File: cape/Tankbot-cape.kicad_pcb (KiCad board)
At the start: 2 copper layers, 54.6 x 86.4 mm, 17 parts, among them J1 MOTOR_RIBBON, J2 Battery, J3 Regulator connector, J4 JUMP TO DISABLE REGULATOR, J5 Qwiic Connector, P8 BeagleBone_Black_Header, P9 BeagleBone_Black_Header

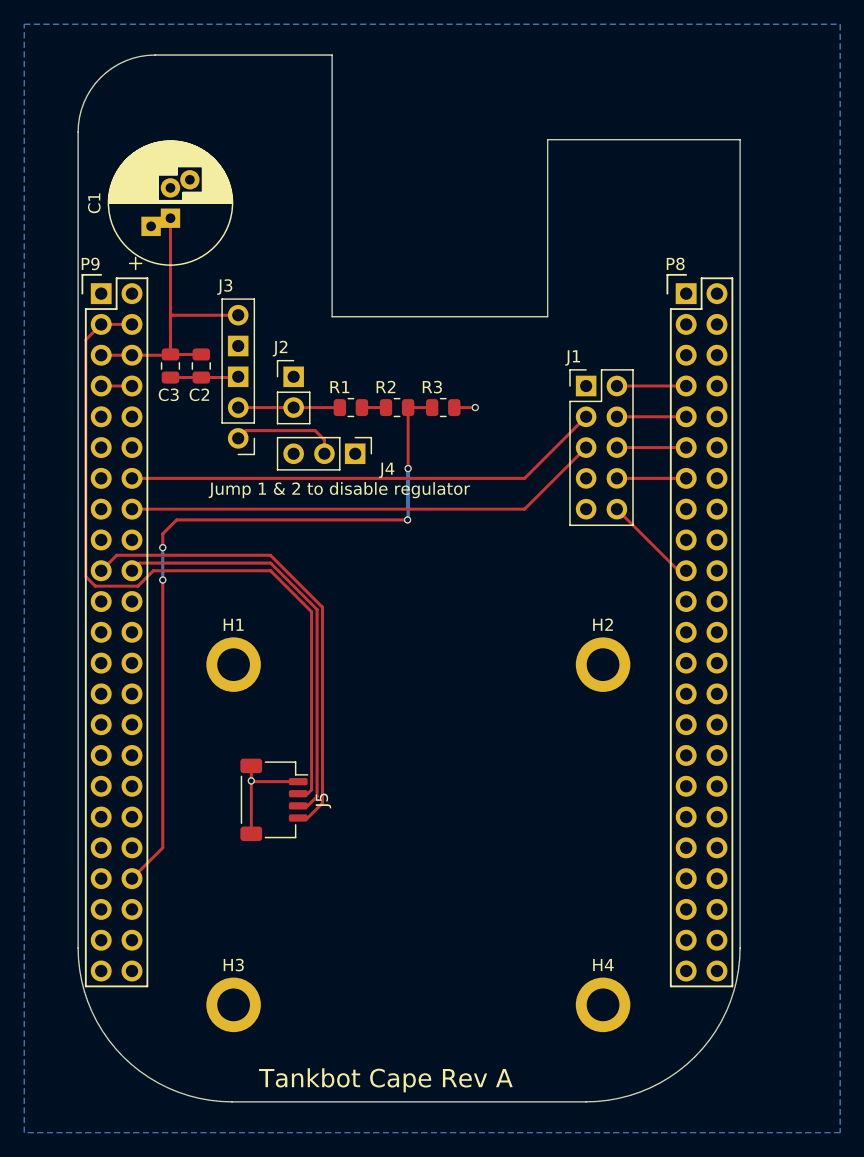
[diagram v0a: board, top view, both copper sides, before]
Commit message: Dropped regulator disable, fixed battery footprint, etc
1. I removed the regulator disable header as I don't think it's necessary.
1. I fixed the battery footprint to be an XT30 connector.
1. I gave the motor ribbon connector a little more clearance to P8.
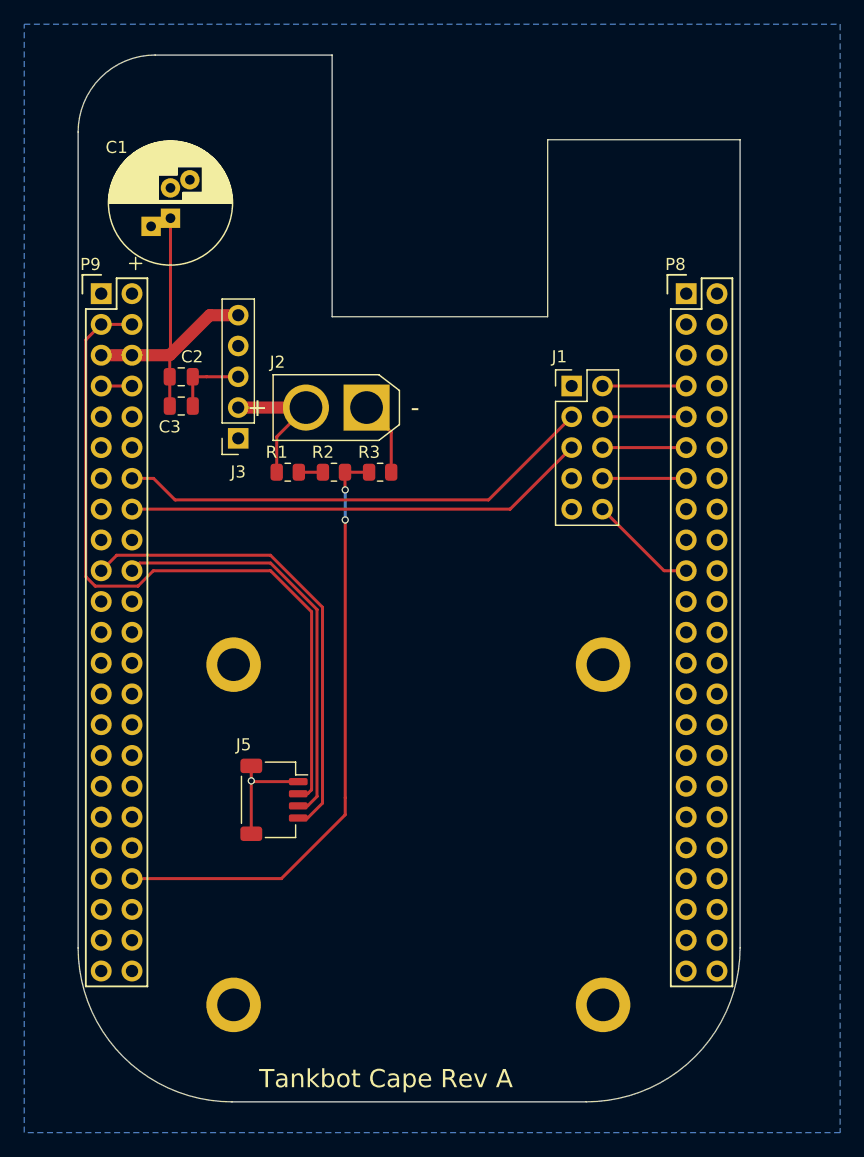
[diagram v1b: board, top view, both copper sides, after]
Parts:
- removed J4: JUMP TO DISABLE REGULATOR, Connector_PinHeader_2.54mm:PinHeader_1x03_P2.54mm_Vertical
- J2: footprint Connector_PinHeader_2.54mm:PinHeader_1x02_P2.54mm_Vertical -> Connector_AMASS:AMASS_XT30U-M_1x02_P5.0mm_Vertical
- J3: footprint Connector_PinHeader_2.54mm:PinHeader_1x05_P2.54mm_Vertical -> Connector_PinSocket_2.54mm:PinSocket_1x05_P2.54mm_Vertical
- moved R3 7.45 mm to (139.4, 77.1)
- moved R1 7.45 mm to (131.8, 77.1)
- moved R2 7.45 mm to (135.6, 77.1)
- moved J2 6.53 mm to (138.3, 71.8), turned to 180 degrees
- moved C3 3.42 mm to (123.0, 71.7), turned to 0 degrees
- moved C2 1.88 mm to (123.0, 69.2), turned to 0 degrees
- moved J1 1.19 mm to (155.2, 70.0)
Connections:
- J3 pad 1: REGULATOR_ENABLE -> Net-(J3-Pad1)
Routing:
- net VBAT_MEASURE: track 64.9 -> 50.0 mm, vias 4 -> 2
- net REGULATOR_ENABLE: track 8.83 -> 0.00 mm
- net GNDD: track 17.0 -> 22.2 mm, vias 2 -> 1
- net +BATT: track 8.38 -> 11.9 mm
- net MOTOR_RIGHT_B: track 7.82 -> 9.65 mm
- net +5V: track 29.6 -> 31.2 mm
- net MOTOR_LEFT_B: track 39.6 -> 38.4 mm
- net MOTOR_nSLEEP: track 5.72 -> 6.91 mm
- net MOTOR_nFAULT: track 5.72 -> 6.91 mm
- net MOTOR_RIGHT_A: track 5.72 -> 6.91 mm
- net MOTOR_PWR_EN: track 5.72 -> 6.91 mm
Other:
- board text removed: "Jump 1 & 2 to disable regulator"

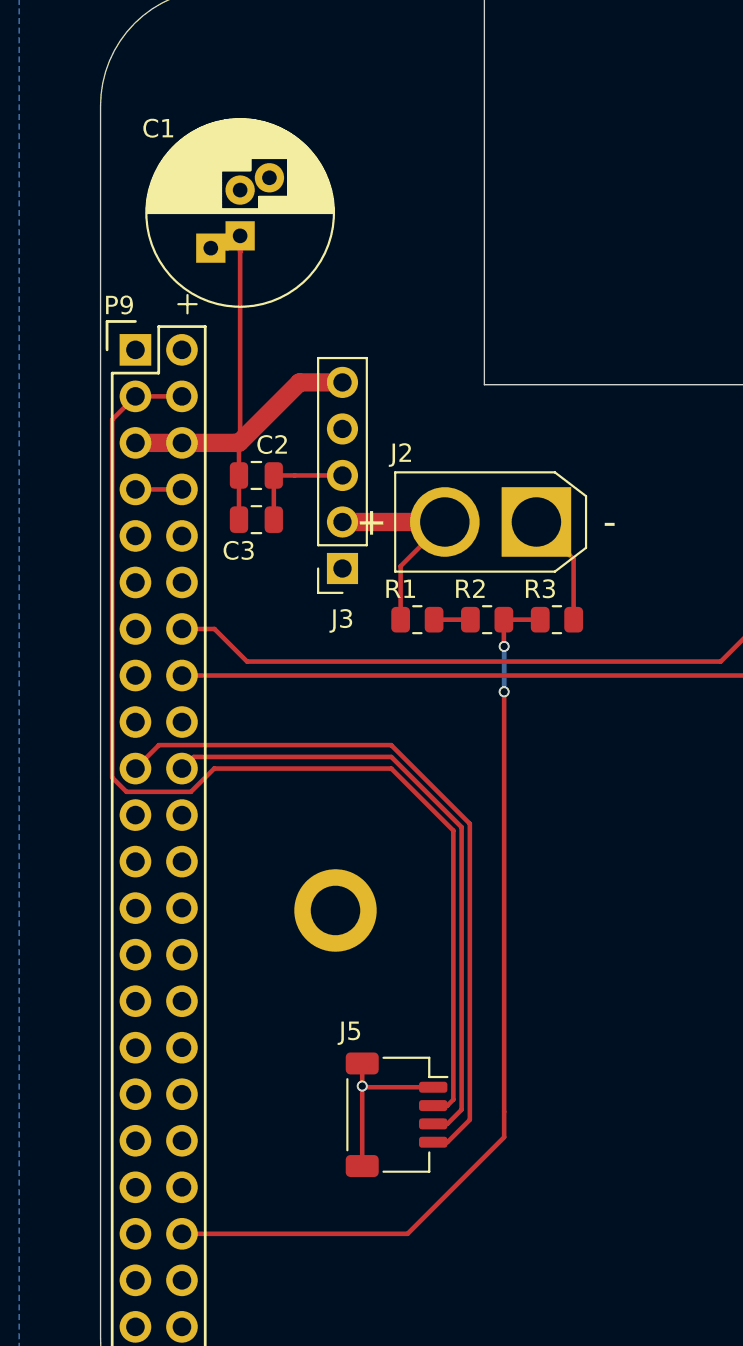
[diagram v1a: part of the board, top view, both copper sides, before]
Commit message: Changed battery board-to-board connector to Molex KK 254
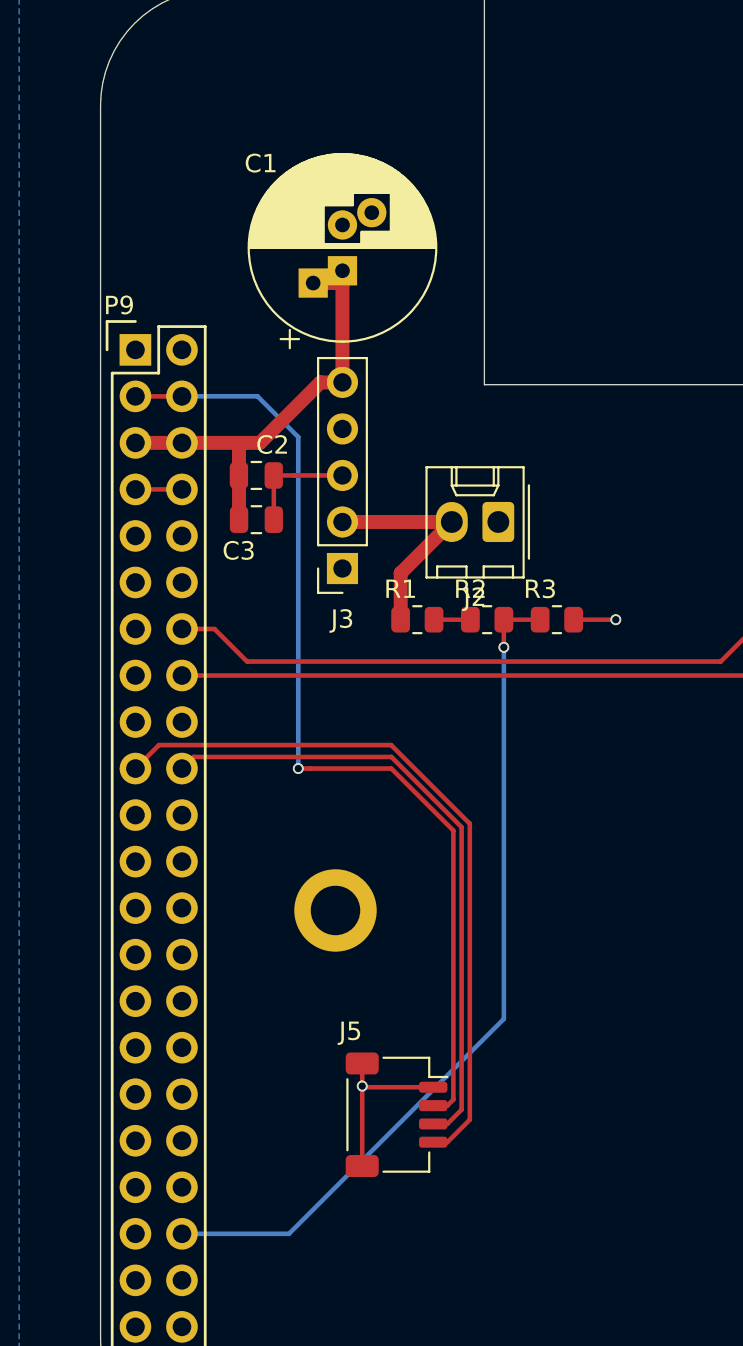
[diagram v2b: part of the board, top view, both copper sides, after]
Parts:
- J1: value MOTOR_RIBBON -> Motor Ribbon
- J2: footprint Connector_AMASS:AMASS_XT30U-M_1x02_P5.0mm_Vertical -> Connector_Molex:Molex_KK-254_AE-6410-02A_1x02_P2.54mm_Vertical
- moved C1 5.90 mm to (127.7, 58.1)
- moved J2 2.08 mm to (136.2, 71.8)
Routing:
- net +3V3: track 60.7 -> 53.7 mm, vias 0 -> 1
- net +5V: track 31.2 -> 24.7 mm
- net GNDD: track 22.2 -> 18.3 mm, vias 1 -> 2
- net VBAT_MEASURE: track 50.0 -> 46.2 mm, vias 2 -> 1
- net +BATT: track 11.9 -> 12.5 mm
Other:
- net class Power added: clearance 0.381, trace_width 0.762, via_dia 0.6, via_drill 0.4

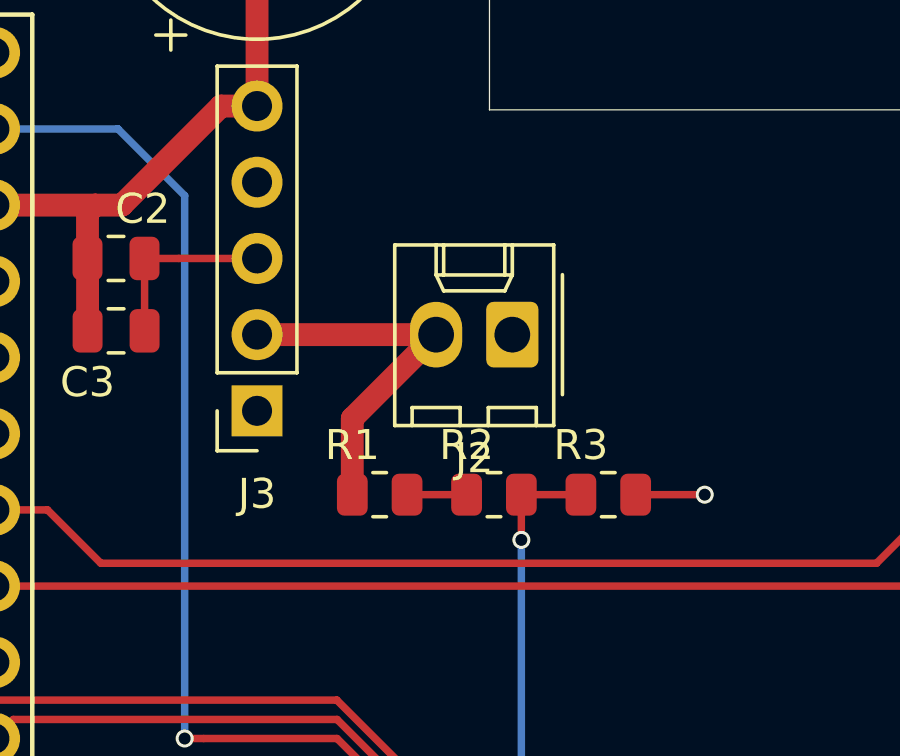
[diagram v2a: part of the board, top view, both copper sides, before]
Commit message: Updated b2b power connector to 4-pin
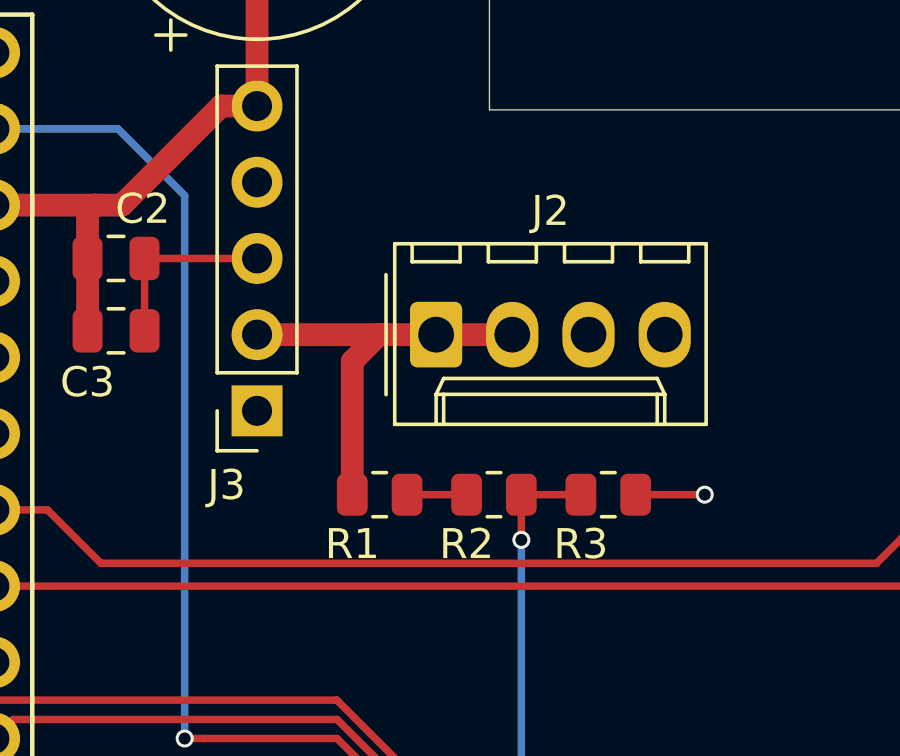
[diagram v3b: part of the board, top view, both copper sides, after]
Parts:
- J2: value Battery -> Conn_01x04; footprint Connector_Molex:Molex_KK-254_AE-6410-02A_1x02_P2.54mm_Vertical -> Connector_Molex:Molex_KK-254_AE-6410-04A_1x04_P2.54mm_Vertical
- moved J2 2.54 mm to (133.6, 71.8), turned to 0 degrees
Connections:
- J2 pad 1: GNDD -> +BATT
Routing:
- net +BATT: track 12.5 -> 14.2 mm

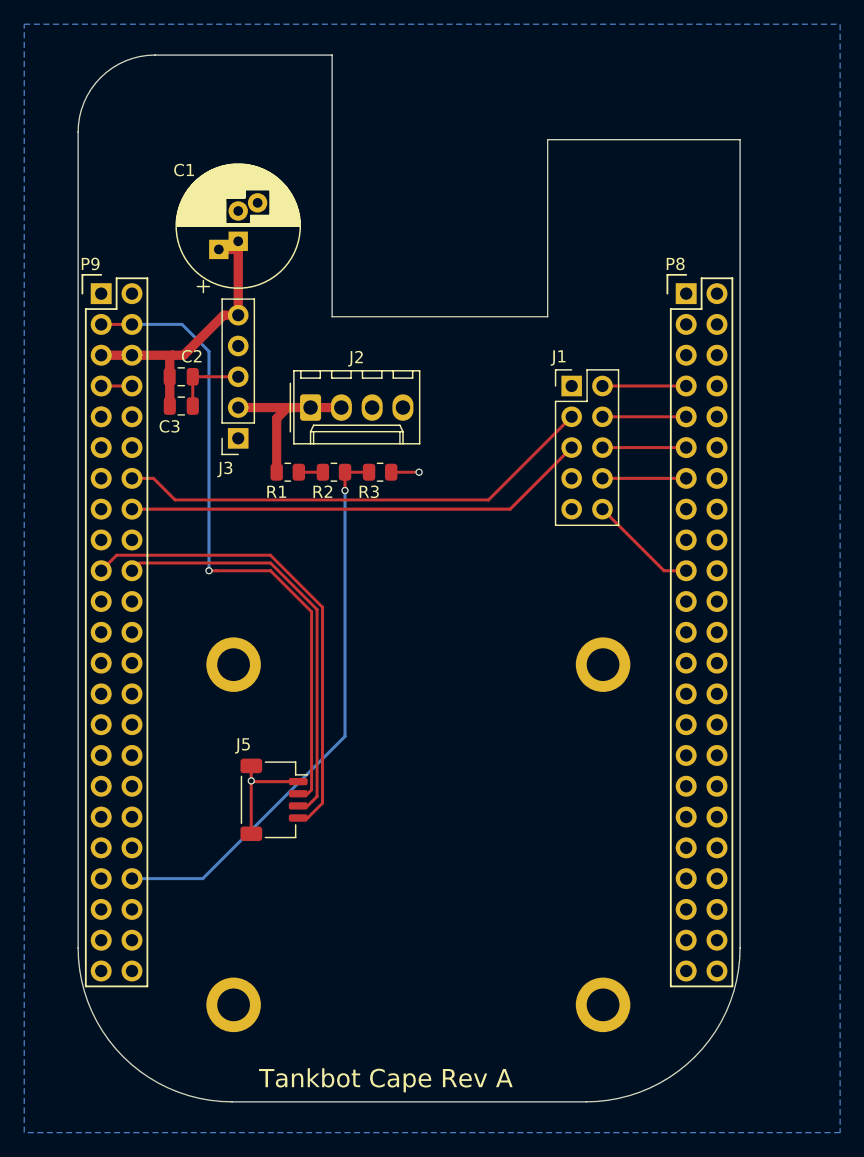
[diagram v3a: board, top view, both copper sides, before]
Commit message: Added shutdown button to the cape
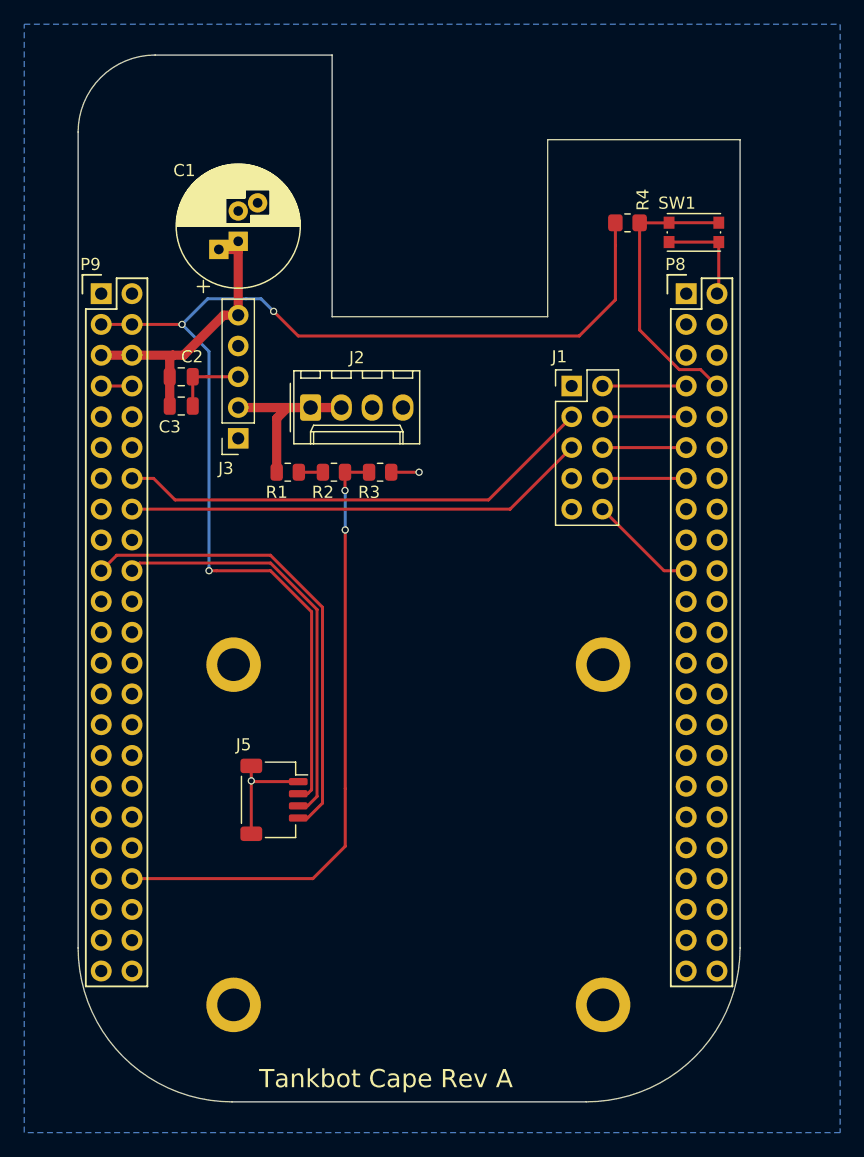
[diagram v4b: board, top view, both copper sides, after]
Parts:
- added R4: R, Resistor_SMD:R_0805_2012Metric_Pad1.20x1.40mm_HandSolder, F.Cu at (159.8, 56.5)
- added SW1: SW_Push, Button_Switch_SMD:SW_Push_1P1T_NO_CK_KMR2, F.Cu at (165.3, 57.3)
- J2: value Conn_01x04 -> BoardToBoardPower
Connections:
- net PWR_BUT renamed Net-(P9-Pad9)
- net SYS_RESETN renamed Net-(P9-Pad10)
- P8 pad 8: Net-(P8-Pad8) -> BTN_SHUTDOWN
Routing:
- net +3V3: track 53.7 -> 99.2 mm, vias 1 -> 3
- net BTN_SHUTDOWN: track 0.00 -> 23.7 mm
- net GNDD: track 18.3 -> 26.2 mm
- net VBAT_MEASURE: track 46.2 -> 51.6 mm, vias 1 -> 2
